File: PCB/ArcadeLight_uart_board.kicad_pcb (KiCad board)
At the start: 2 copper layers, 52.4 x 77.1 mm, 20 parts, among them J1 Partition_Lights_L, J10 Circle_LED, J11 Cross_LED, J12 Square_LED, J13 Triangle_LED, J3 12V_In, J9 Partition_Lights_R, P7 CONN_01X01, P9 CONN_01X01, Q1 AO3404A, Q2 IRFR9024N, U2 ULN2003, U6 ULN2003

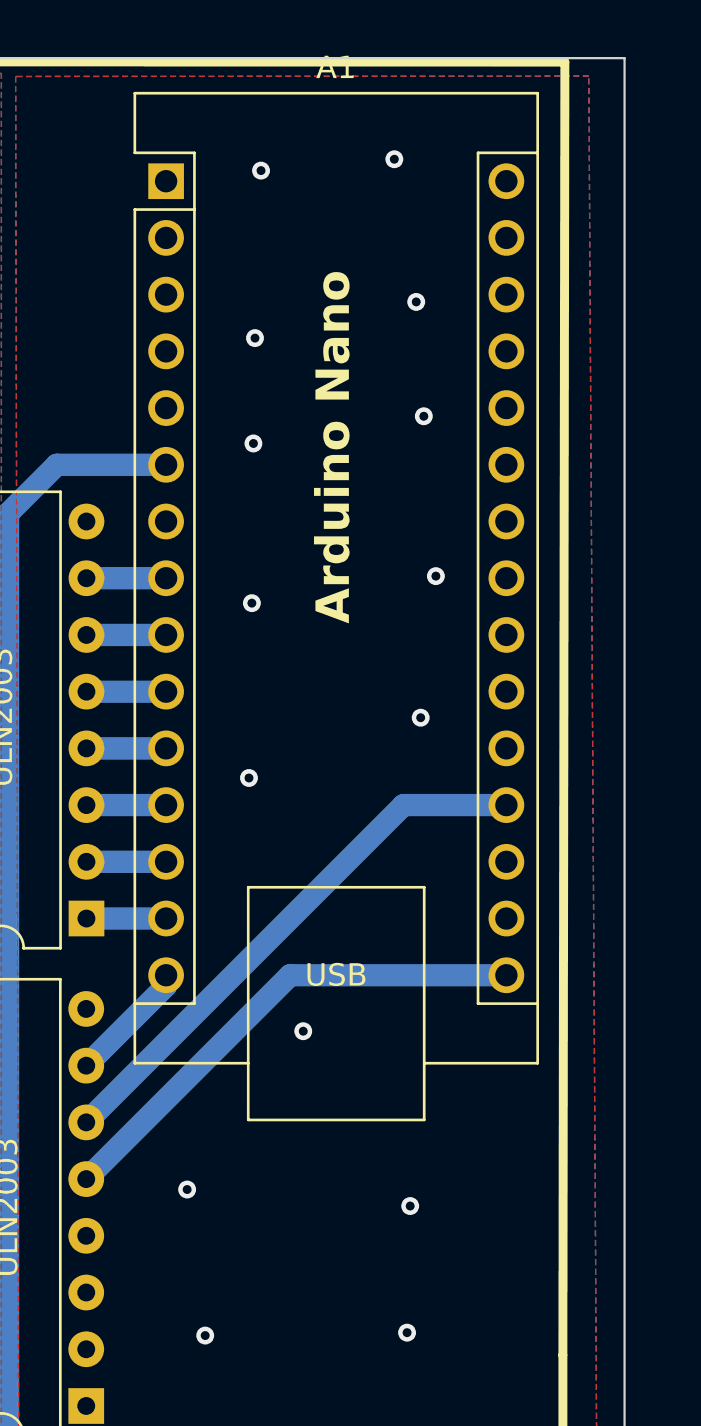
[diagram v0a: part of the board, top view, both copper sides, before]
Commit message: Arduino program PWM brightness control added
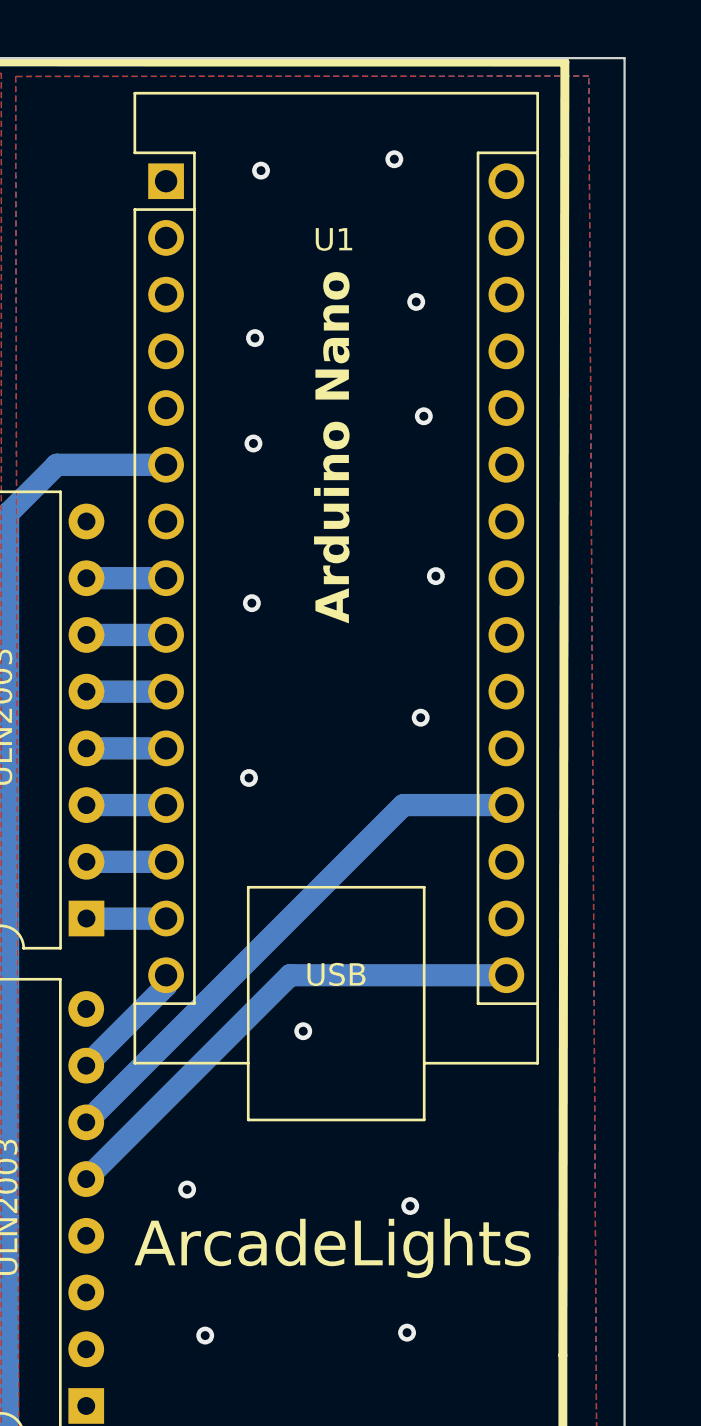
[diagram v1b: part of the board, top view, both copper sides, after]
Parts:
- renumbered A1 to U1, U6 to U3
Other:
- board text added: "ArcadeLights"

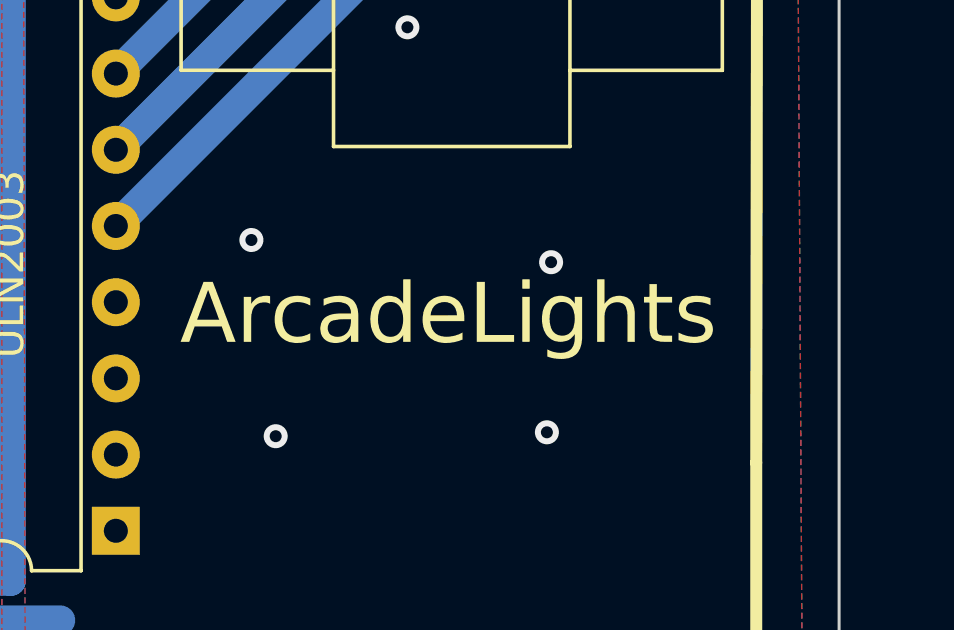
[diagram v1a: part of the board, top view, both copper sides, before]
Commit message: R1 fix to 1k
10k do not work
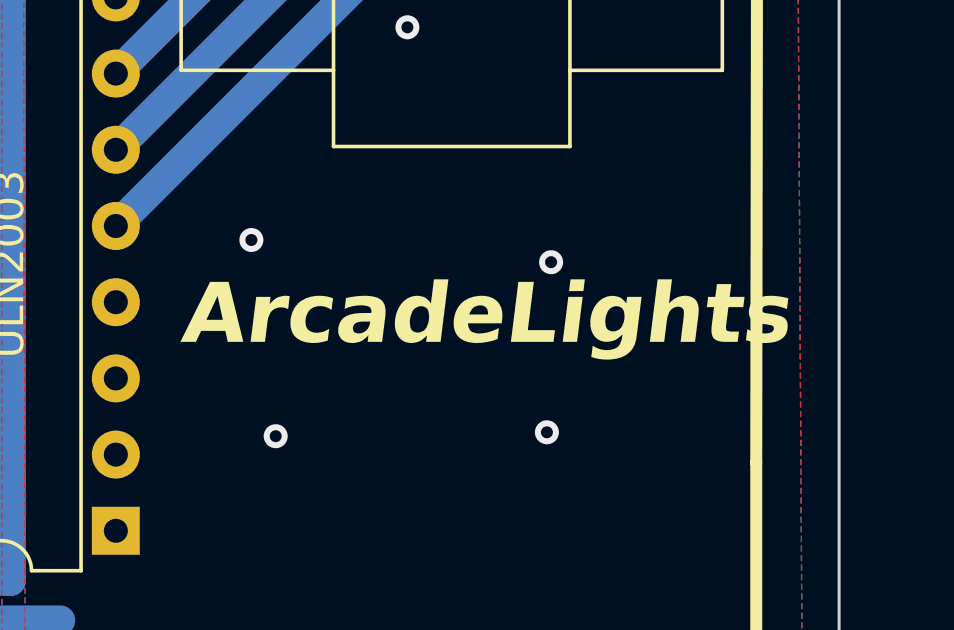
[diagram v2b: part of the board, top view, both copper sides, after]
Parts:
- R2: value 10k -> 1k
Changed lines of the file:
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@@
       (effects (font (size 1 1) (thickness 0.15)))
     )
-    (fp_text value "10k" (at 0 1.82 -180) (layer "F.Fab")
+    (fp_text value "1k" (at 0 1.82 -180) (layer "F.Fab")
       (effects (font (size 1 1) (thickness 0.15)))
     )
@@
   )
   (gr_text "ArcadeLights" (at 212.44 94.77) (layer "F.SilkS")
-    (effects (font (size 2 2) (thickness 0.3)) (justify left bottom))
+    (effects (font (size 2 2) (thickness 0.4) bold italic) (justify left bottom))
   )
   (gr_text "Cross" (at 191.444 50.042 90) (layer "F.SilkS")

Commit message: Readme update
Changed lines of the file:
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@@
     (stroke (width 0.15) (type default)) (fill none) (layer "F.SilkS"))
   (gr_line (start 192.151 97.282) (end 201.93 97.282)
-    (stroke (width 0.15) (type default)) (layer "F.SilkS"))
+    (stroke (width 0.4) (type default)) (layer "F.SilkS"))
   (gr_rect (start 188.528 69.222) (end 200.42 97.162)
     (stroke (width 0.15) (type default)) (fill none) (layer "F.SilkS"))
@@
     (stroke (width 0.4) (type default)) (layer "F.SilkS"))
   (gr_line (start 201.93 97.282) (end 201.93 104.648)
-    (stroke (width 0.15) (type default)) (layer "F.SilkS"))
+    (stroke (width 0.4) (type default)) (layer "F.SilkS"))
   (gr_line (start 231.648 98.552) (end 231.648 104.76)
     (stroke (width 0.4) (type default)) (layer "F.SilkS"))
@@
     (stroke (width 0.4) (type default)) (layer "F.SilkS"))
   (gr_line (start 182.5625 97.282) (end 192.3415 97.282)
-    (stroke (width 0.15) (type default)) (layer "F.SilkS"))
+    (stroke (width 0.4) (type default)) (layer "F.SilkS"))
   (gr_rect (start 182.04 40.462) (end 234.41 117.545)
     (stroke (width 0.1) (type default)) (fill none) (layer "Edge.Cuts"))
